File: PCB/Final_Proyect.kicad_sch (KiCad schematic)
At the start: 38 parts, among them J1 Conn_01x10_Pin, J2 VCC GND TTP223, J3 OLLED I2C, J4 - +, J5 USB_C, U1 ESP32-S3-WROOM-1, U2 AMS1117-3.3

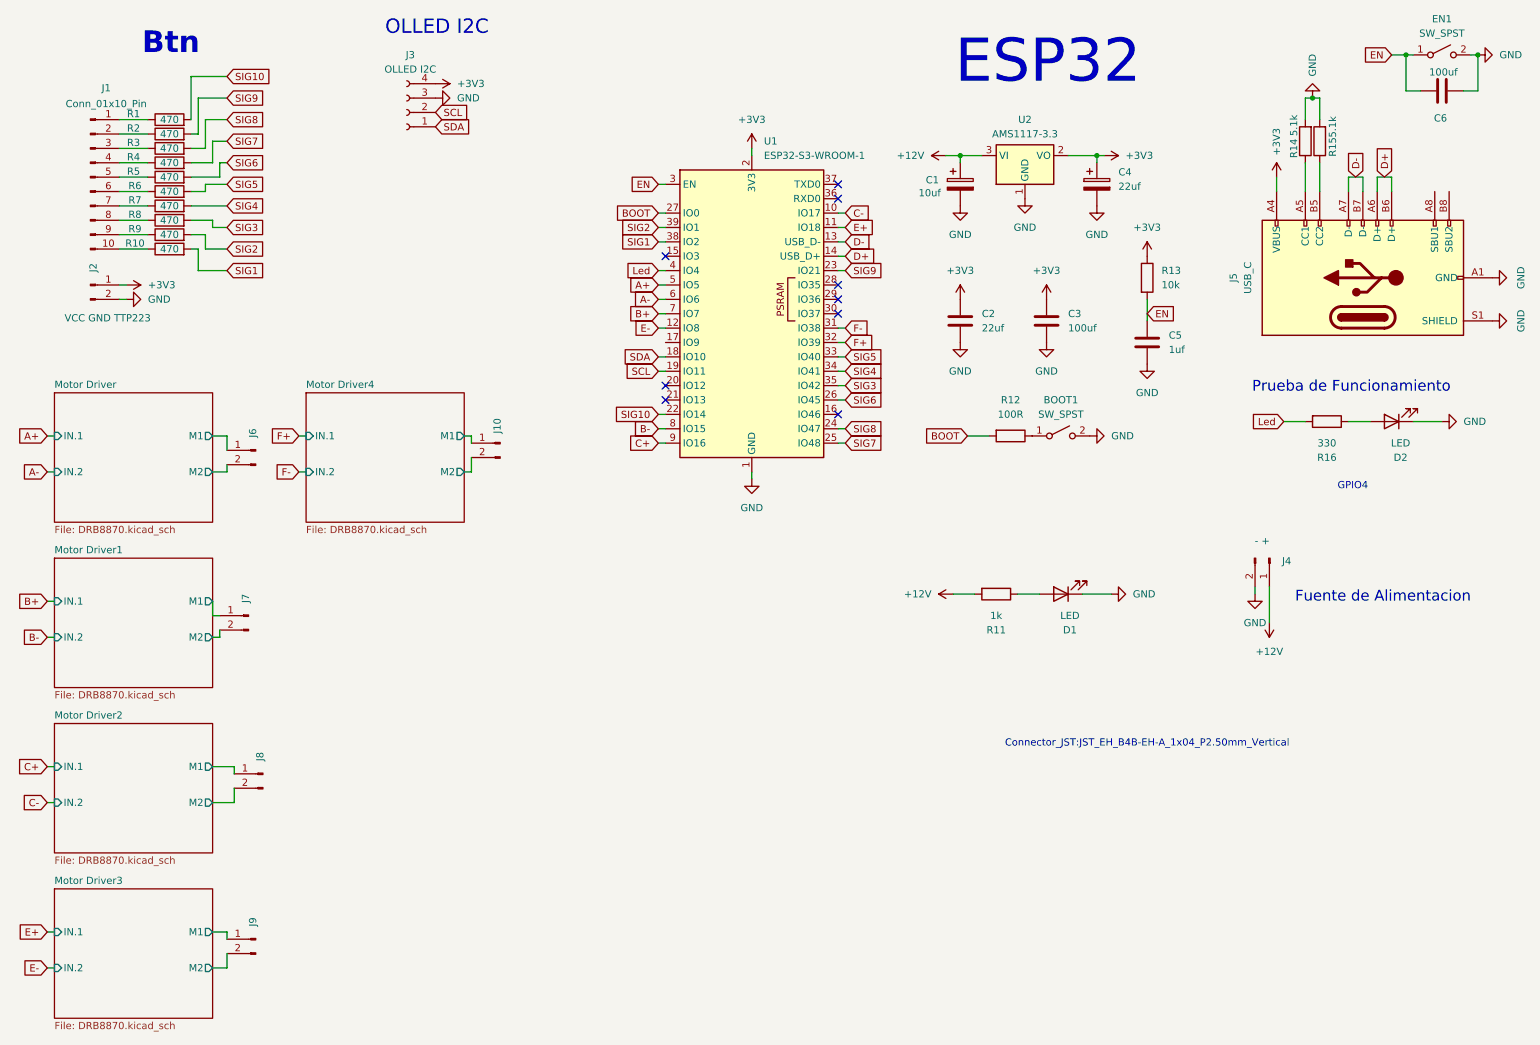
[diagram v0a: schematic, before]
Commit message: Enrutamiento mejorado
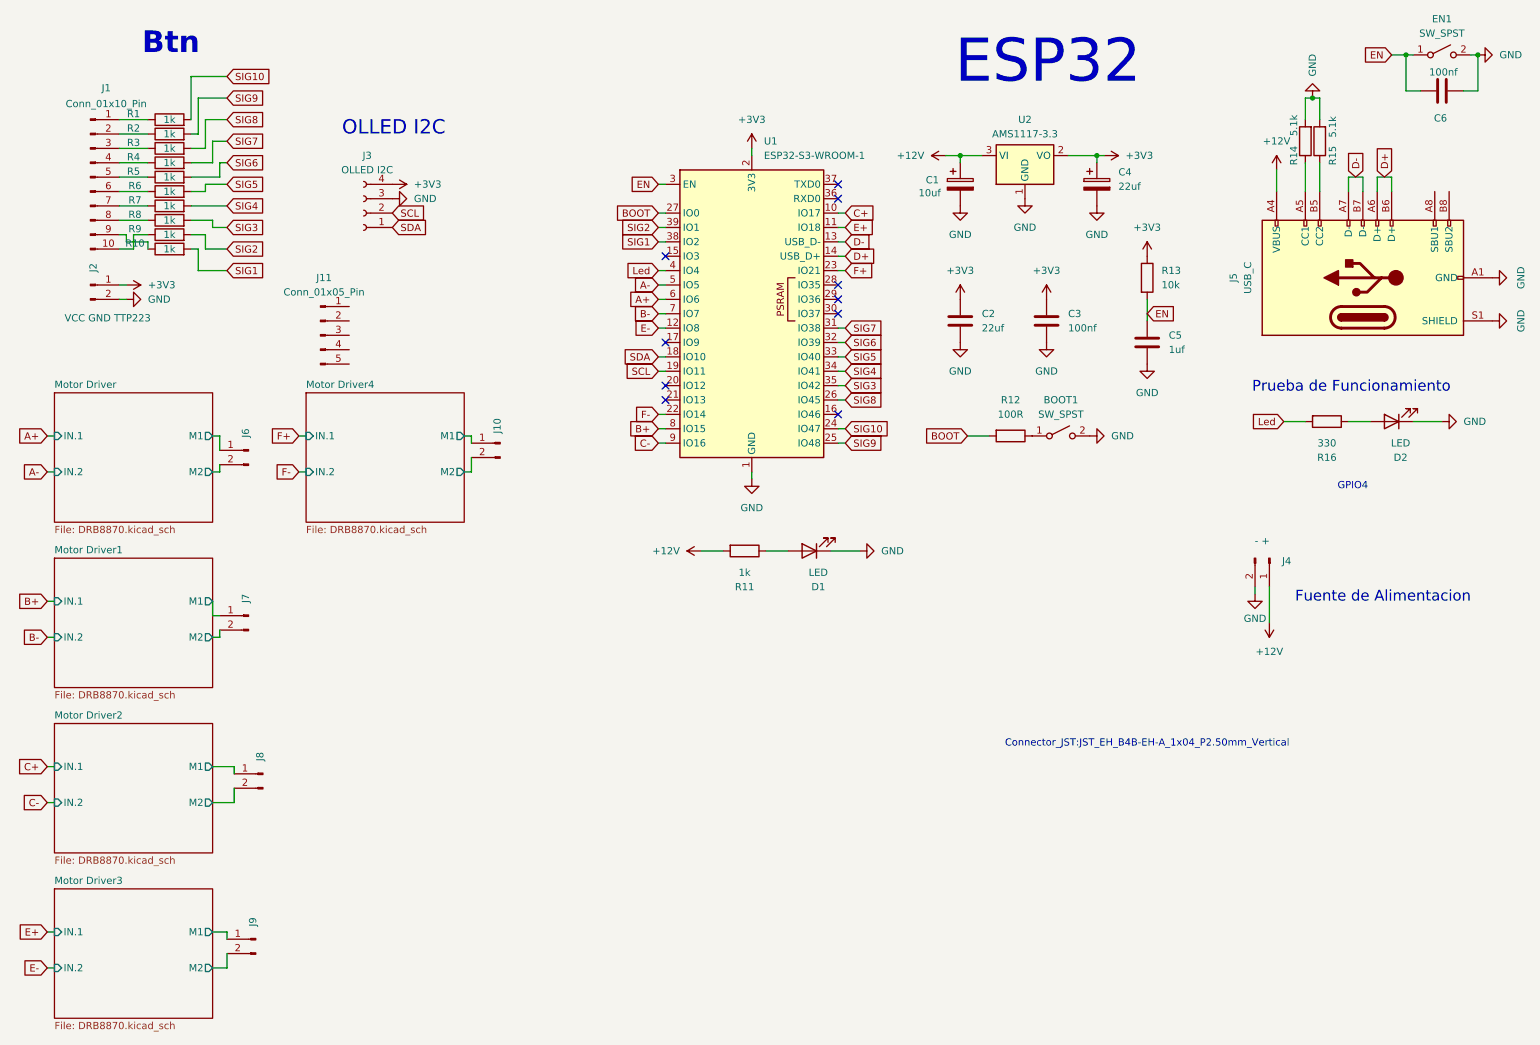
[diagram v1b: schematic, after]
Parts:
- added J11: Conn_01x05_Pin, Connector_JST:JST_EH_B5B-EH-A_1x05_P2.50mm_Vertical, symbol Connector:Conn_01x05_Pin
- BOOT1, EN1: LCSC (none) -> C49234124
- C1: footprint Capacitor_SMD:C_0603_1608Metric -> Capacitor_SMD:C_0805_2012Metric; LCSC (none) -> C15850
- C2, C4: footprint Capacitor_SMD:C_0603_1608Metric -> Capacitor_SMD:C_0805_2012Metric; LCSC (none) -> C602037
- C3, C6: value 100uf -> 100nf; footprint Capacitor_SMD:C_0603_1608Metric -> Capacitor_SMD:C_0805_2012Metric; LCSC (none) -> C519981
- C5: footprint Capacitor_SMD:C_0603_1608Metric -> Capacitor_SMD:C_0805_2012Metric; LCSC (none) -> C116352
- D1: LCSC (none) -> C965799
- D2: LCSC (none) -> C965807
- J1, J10, J2, J3, J4, J6, J7, J8, J9: now left out of the parts list
- J5: LCSC (none) -> C2988369
- R1, R10, R2, R3, R4, R5, R6, R7, R8, R9: value 470 -> 1k; LCSC (none) -> C2907232
- R11: LCSC (none) -> C2907232
- R12: LCSC (none) -> C17408
- R14, R15: LCSC (none) -> C27834
- R16: LCSC (none) -> C2930157
- U1: LCSC (none) -> C2913198
- U2: LCSC (none) -> C347222
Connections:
- net +12V: now also J5.A4 (VBUS), J5.A9 (VBUS), J5.B4 (VBUS), J5.B9 (VBUS)
- net +3V3: no longer J5.A4 (VBUS), J5.A9 (VBUS), J5.B4 (VBUS), J5.B9 (VBUS)
- net A+: now also U1.6 (IO6); no longer U1.5 (IO5)
- net A-: now also U1.5 (IO5); no longer U1.6 (IO6)
- net B+: now also U1.8 (IO15); no longer U1.7 (IO7)
- net B-: now also U1.7 (IO7); no longer U1.8 (IO15)
- net C+: now also U1.10 (IO17); no longer U1.9 (IO16)
- net C-: now also U1.9 (IO16); no longer U1.10 (IO17)
- net F+: now also U1.23 (IO21); no longer U1.32 (IO39)
- net F-: now also U1.22 (IO14); no longer U1.31 (IO38)
- net SIG10: now also U1.24 (IO47); no longer U1.22 (IO14)
- net SIG6: now also U1.32 (IO39); no longer U1.26 (IO45)
- net SIG7: now also U1.31 (IO38); no longer U1.25 (IO48)
- net SIG8: now also U1.26 (IO45); no longer U1.24 (IO47)
- net SIG9: now also U1.25 (IO48); no longer U1.23 (IO21)
- net at R9.1: now also J1.10 (Pin_10); no longer J1.9 (Pin_9)
- net at R10.1: now also J1.9 (Pin_9); no longer J1.10 (Pin_10)
- no-connect marks 9 -> 10
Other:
- moved on the sheet: D1, J3, J6, R11

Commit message: Finalizado
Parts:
- removed J11: Conn_01x05_Pin, Connector_JST:JST_EH_B5B-EH-A_1x05_P2.50mm_Vertical, symbol Connector:Conn_01x05_Pin
- added C22: 220uF, Capacitor_SMD:CP_Elec_6.3x7.7, symbol Device:C_Polarized
- added C23: 100uf, Capacitor_SMD:C_0805_2012Metric, symbol Device:C_Polarized
- added D3: SS18, Diode_SMD:D_SMA, symbol Diode:SS18
- C1: LCSC C15850 -> C17024
- C2, C4: LCSC C602037 -> C29277
- C3, C6: LCSC C519981 -> C710980
- C5: LCSC C116352 -> C650988
- D2: LCSC C965807 -> C7496819
- J5: LCSC C2988369 -> C2765186
- R1, R10, R11, R2, R3, R4, R5, R6, R7, R8, R9: LCSC C2907232 -> C2907295
- R13: LCSC (none) -> C2930231
- R14, R15: LCSC C27834 -> C2930296
- R16: LCSC C2930157 -> C2907321
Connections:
- net +12V: now also C22.1, D3.1 (K); no longer J4.1 (Pin_1)
- net +3V3: now also C23.1
- net GND: now also C22.2, C23.2
- new net: D3.2 (A), J4.1 (Pin_1)
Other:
- moved on the sheet: J4
